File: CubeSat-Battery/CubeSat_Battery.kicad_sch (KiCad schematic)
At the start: 3 parts, among them J1 Conn_01x02_Pin, J2 Screw_Terminal_01x02, U1 BatteryPack

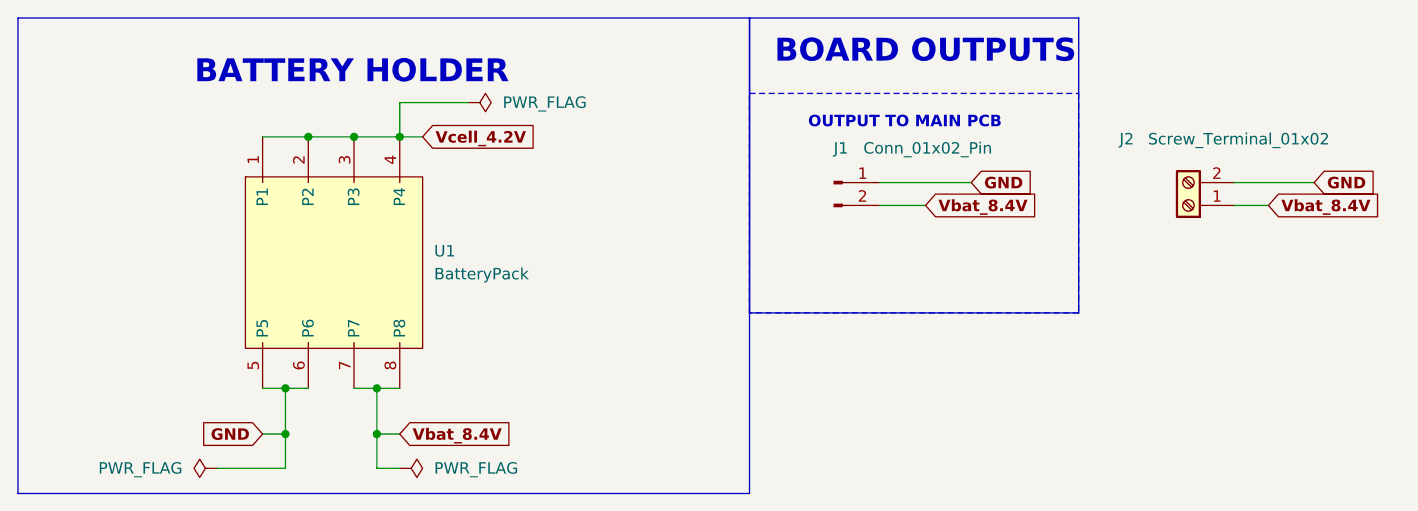
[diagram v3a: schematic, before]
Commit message: new Main and EPS PCBs, all previous problems corrected, final version
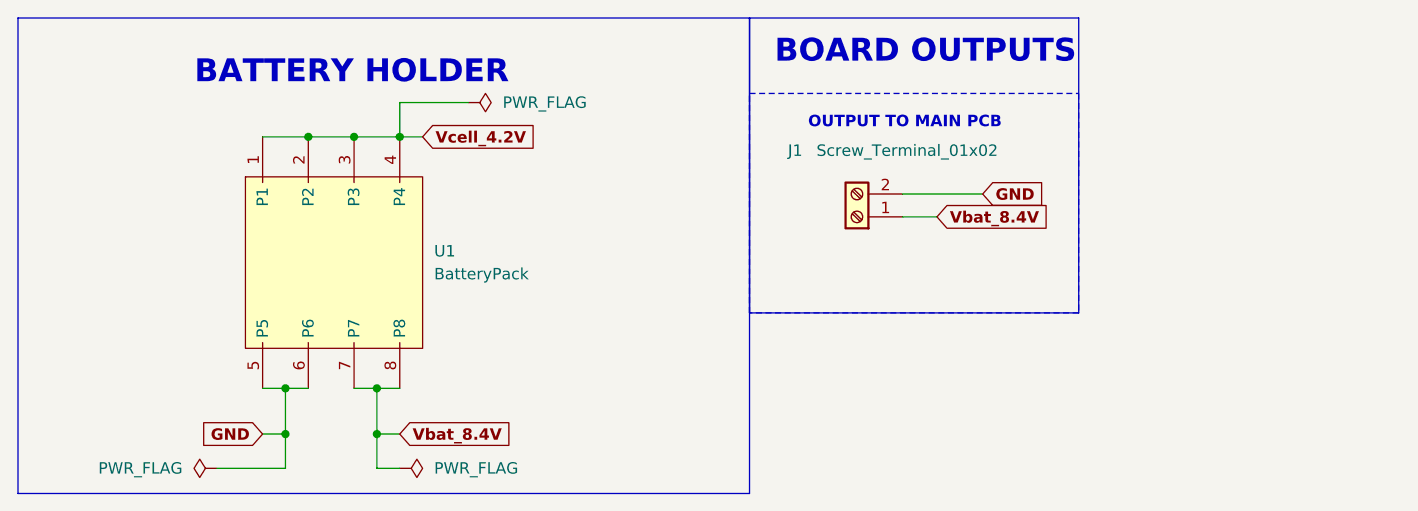
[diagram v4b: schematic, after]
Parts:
- removed J1: Conn_01x02_Pin, Connector_JST:JST_EH_B2B-EH-A_1x02_P2.50mm_Vertical, symbol Connector:Conn_01x02_Pin
- renumbered J2 to J1
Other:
- moved on the sheet: J1
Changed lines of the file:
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@@
 	(wire
 		(pts
-			(xy 147.32 30.48) (xy 156.21 30.48)
-		)
-		(stroke
-			(width 0)
-			(type default)
-		)
-	)
-	(wire
-		(pts
-			(xy 107.95 33.02) (xy 113.03 33.02)
+			(xy 110.49 31.75) (xy 119.38 31.75)
 		)
 		(stroke
@@
 	(wire
 		(pts
-			(xy 147.32 33.02) (xy 151.13 33.02)
-		)
-		(stroke
-			(width 0)
-			(type default)
-		)
-	)
-	(wire
-		(pts
-			(xy 107.95 30.48) (xy 118.11 30.48)
+			(xy 110.49 34.29) (xy 114.3 34.29)
 		)
 		(stroke
@@
 	(global_label "Vbat_8.4V"
 		(shape input)
-		(at 151.13 33.02 0)
+		(at 114.3 34.29 0)
 		(fields_autoplaced yes)
 		(effects
@@
 		)
 		(property "Intersheetrefs" "${INTERSHEET_REFS}"
-			(at 163.7835 33.02 0)
+			(at 126.9535 34.29 0)
 			(effects
 				(font
@@
 	(global_label "GND"
 		(shape input)
-		(at 156.21 30.48 0)
+		(at 119.38 31.75 0)
 		(fields_autoplaced yes)
 		(effects
@@
 		)
 		(property "Intersheetrefs" "${INTERSHEET_REFS}"
-			(at 163.5417 30.48 0)
-			(effects
-				(font
-					(size 1.27 1.27)
-				)
-				(justify left)
-				(hide yes)
-			)
-		)
-	)
-	(global_label "GND"
-		(shape input)
-		(at 118.11 30.48 0)
-		(fields_autoplaced yes)
-		(effects
-			(font
-				(size 1.27 1.27)
-				(thickness 0.254)
-				(bold yes)
-			)
-			(justify left)
-		)
-		(property "Intersheetrefs" "${INTERSHEET_REFS}"
-			(at 125.4417 30.48 0)
-			(effects
-				(font
-					(size 1.27 1.27)
-				)
-				(justify left)
-				(hide yes)
-			)
-		)
-	)
-	(global_label "Vbat_8.4V"
-		(shape input)
-		(at 113.03 33.02 0)
-		(fields_autoplaced yes)
-		(effects
-			(font
-				(size 1.27 1.27)
-				(thickness 0.254)
-				(bold yes)
-			)
-			(justify left)
-		)
-		(property "Intersheetrefs" "${INTERSHEET_REFS}"
-			(at 125.6835 33.02 0)
-			(effects
-				(font
-					(size 1.27 1.27)
-				)
-				(justify left)
-				(hide yes)
-			)
-		)
-	)
-	(symbol
-		(lib_id "Connector:Conn_01x02_Pin")
-		(at 102.87 30.48 0)
-		(unit 1)
-		(exclude_from_sim no)
-		(in_bom yes)
-		(on_board yes)
-		(dnp no)
-		(property "Reference" "J1"
-			(at 103.632 26.67 0)
-			(effects
-				(font
-					(size 1.27 1.27)
-				)
-			)
-		)
-		(property "Value" "Conn_01x02_Pin"
-			(at 113.284 26.67 0)
-			(effects
-				(font
-					(size 1.27 1.27)
-				)
-			)
-		)
-		(property "Footprint" "Connector_JST:JST_EH_B2B-EH-A_1x02_P2.50mm_Vertical"
-			(at 102.87 30.48 0)
-			(effects
-				(font
-					(size 1.27 1.27)
-				)
-				(hide yes)
-			)
-		)
-		(property "Datasheet" "~"
-			(at 102.87 30.48 0)
-			(effects
-				(font
-					(size 1.27 1.27)
-				)
-				(hide yes)
-			)
-		)
-		(property "Description" "Generic connector, single row, 01x02, script generated"
-			(at 102.87 30.48 0)
-			(effects
-				(font
-					(size 1.27 1.27)
-				)
-				(hide yes)
-			)
-		)
-		(pin "1"
-		)
-		(pin "2"
-		)
-		(instances
-			(project "Cubesat_EPS"
-				(path "/b0f59bc3-d31e-43eb-8cb8-cd4747043e73"
-					(reference "J1")
-					(unit 1)
-				)
+			(at 126.7117 31.75 0)
+			(effects
+				(font
+					(size 1.27 1.27)
+				)
+				(justify left)
+				(hide yes)
 			)
 		)
@@
 	(symbol
 		(lib_id "Connector:Screw_Terminal_01x02")
-		(at 142.24 33.02 180)
+		(at 105.41 34.29 180)
 		(unit 1)
 		(exclude_from_sim no)
@@
 		(on_board yes)
 		(dnp no)
-		(property "Reference" "J2"
-			(at 135.382 25.654 0)
+		(property "Reference" "J1"
+			(at 98.552 26.924 0)
 			(effects
 				(font
@@
 		)
 		(property "Value" "Screw_Terminal_01x02"
-			(at 147.828 25.654 0)
+			(at 110.998 26.924 0)
 			(effects
 				(font
@@
 		)
 		(property "Footprint" "TerminalBlock_Phoenix:TerminalBlock_Phoenix_MKDS-1,5-2_1x02_P5.00mm_Horizontal"
-			(at 142.24 33.02 0)
+			(at 105.41 34.29 0)
 			(effects
 				(font
@@
 		)
 		(property "Datasheet" "~"
-			(at 142.24 33.02 0)
+			(at 105.41 34.29 0)
 			(effects
 				(font
@@
 		)
 		(property "Description" "Generic screw terminal, single row, 01x02, script generated (kicad-library-utils/schlib/autogen/connector/)"
-			(at 142.24 33.02 0)
+			(at 105.41 34.29 0)
 			(effects
 				(font
@@
 			(project "CubeSat_Battery"
 				(path "/b0f59bc3-d31e-43eb-8cb8-cd4747043e73"
-					(reference "J2")
+					(reference "J1")
 					(unit 1)
 				)
